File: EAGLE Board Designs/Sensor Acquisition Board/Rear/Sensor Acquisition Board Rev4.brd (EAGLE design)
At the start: 149.9 x 50.8 mm, 44 parts, among them J1 CONNECTOR-SENSOR_NF_S_RA_BLACK, J10 JUMPER_1X02_, J2 CONNECTOR-SENSOR_NF_S_RA_BLACK, J3 CONNECTOR-SENSOR_NF_S_RA_BLACK, J4 CONNECTOR-SENSOR_NF_S_RA_BLACK, J5 CONNECTOR-SENSOR_NF_S_RA_BLACK, J6 CONNECTOR-SENSOR_NF_S_RA_BLACK, J7 CONNECTOR-SENSOR_NF_S_RA_BLACK, J8 CONNECTOR-SENSOR_NF_S_RA_BLACK, J9 CONNECTOR-CAN_NF_S_RA_BLACK, U1 VOLTAGE_REGULATOR_SOT223_5V, U3 TCAN1051HQV-Q1

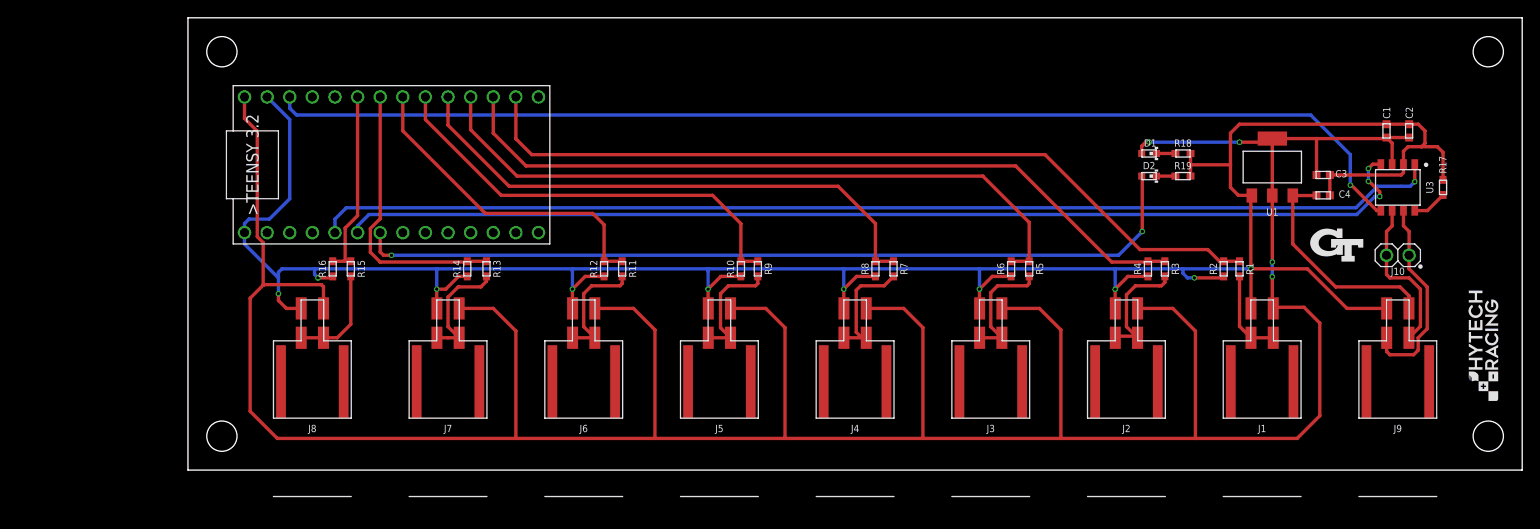
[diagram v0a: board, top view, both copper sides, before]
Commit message: Started on rear board sch
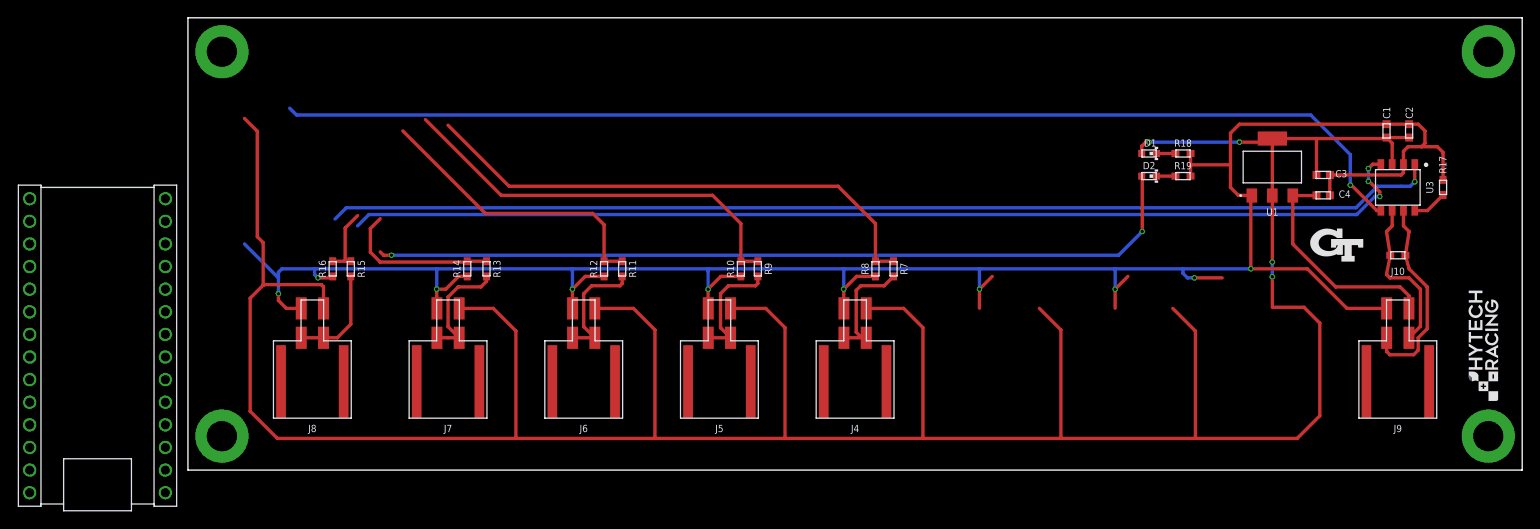
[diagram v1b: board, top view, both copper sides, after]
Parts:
- removed A1: TEENSY_3.2, HyTechDevices:TEENSY_SHORT
- removed J1, J2, J3: CONNECTOR-SENSOR_NF_S_RA_BLACK, HyTechDevices:MOLEX_NANOFIT_SMD_RIGHTANGLE_04
- removed R1, R3, R5: RESISTOR_0603_10K, HyTechDevices:0603-RES
- removed R2, R4, R6: RESISTOR_0603_12K, HyTechDevices:0603-RES
- added A2: TEENSY_4.0, HyTechDevices:TEENSY_SHORT
- J10: value JUMPER_1X02_ -> JUMPER_0603_; device HyTechDevices:1X02 -> HyTechDevices:0603-RES
- U1: value VOLTAGE_REGULATOR_SOT223_5V -> VOLTAGE_REGULATOR_SOT-223_5V; device HyTechDevices:SOT223 -> HyTechDevices:SOT-223
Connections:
- removed net N$10: J2.3, J2.4, R3.2
- removed net N$11: J3.3, J3.4, R5.2
- removed net N$8: J1.3, J1.4, R1.2
- net +5V: now also A2.VIN; no longer A1.VIN, J1.1, J2.1, J3.1
- net CAN_LED: now also A2.D5; no longer A1.D5
- net CAN_RX: now also A2.D4; no longer A1.D4
- net CAN_TX: now also A2.D3; no longer A1.D3
- net GND: now also A2.AGND/GND, A2.GND; no longer A1.AGND/GND, A1.GND, J1.2, J2.2, J3.2, R2.1, R4.1, R6.1
- net SENSOR_1: now also A2.D14; no longer A1.D14, R1.1, R2.2
- net SENSOR_2: now also A2.D15; no longer A1.D15, R3.1, R4.2
- net SENSOR_3: now also A2.D16; no longer A1.D16, R5.1, R6.2
- net SENSOR_4: now also A2.D17; no longer A1.D17
- net SENSOR_5: now also A2.D18; no longer A1.D18
- net SENSOR_6: now also A2.D19; no longer A1.D19
- net SENSOR_7: now also A2.D20; no longer A1.D20
- net SENSOR_8: now also A2.D21; no longer A1.D21
- net TEENSY_3.3V: now also A2.3.3V; no longer A1.3.3V
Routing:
- net SENSOR_1: track 91.7 -> 0.00 mm
- net SENSOR_2: track 85.5 -> 0.00 mm
- net SENSOR_3: track 77.1 -> 0.00 mm
- net GND: track 293.2 -> 263.1 mm
- net SENSOR_7: track 31.4 -> 17.8 mm
- net N$11: track 13.6 -> 0.00 mm
- net SENSOR_8: track 21.1 -> 7.78 mm
- net N$10: track 13.3 -> 0.00 mm
- net +5V: track 360.8 -> 349.8 mm
- net N$8: track 9.93 -> 0.00 mm
- net SENSOR_6: track 36.9 -> 33.1 mm
- net SENSOR_4: track 62.0 -> 58.8 mm
- net SENSOR_5: track 48.9 -> 46.4 mm
- net CAN_LED: track 95.3 -> 93.1 mm
- net CAN_TX: track 126.5 -> 125.0 mm
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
